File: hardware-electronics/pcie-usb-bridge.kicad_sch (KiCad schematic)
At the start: 41 parts, among them U10 24AA04T-I_OT, U3 PI7C9X440SLBFDE, Y1 ABM8-12.000MHZ-B2-T

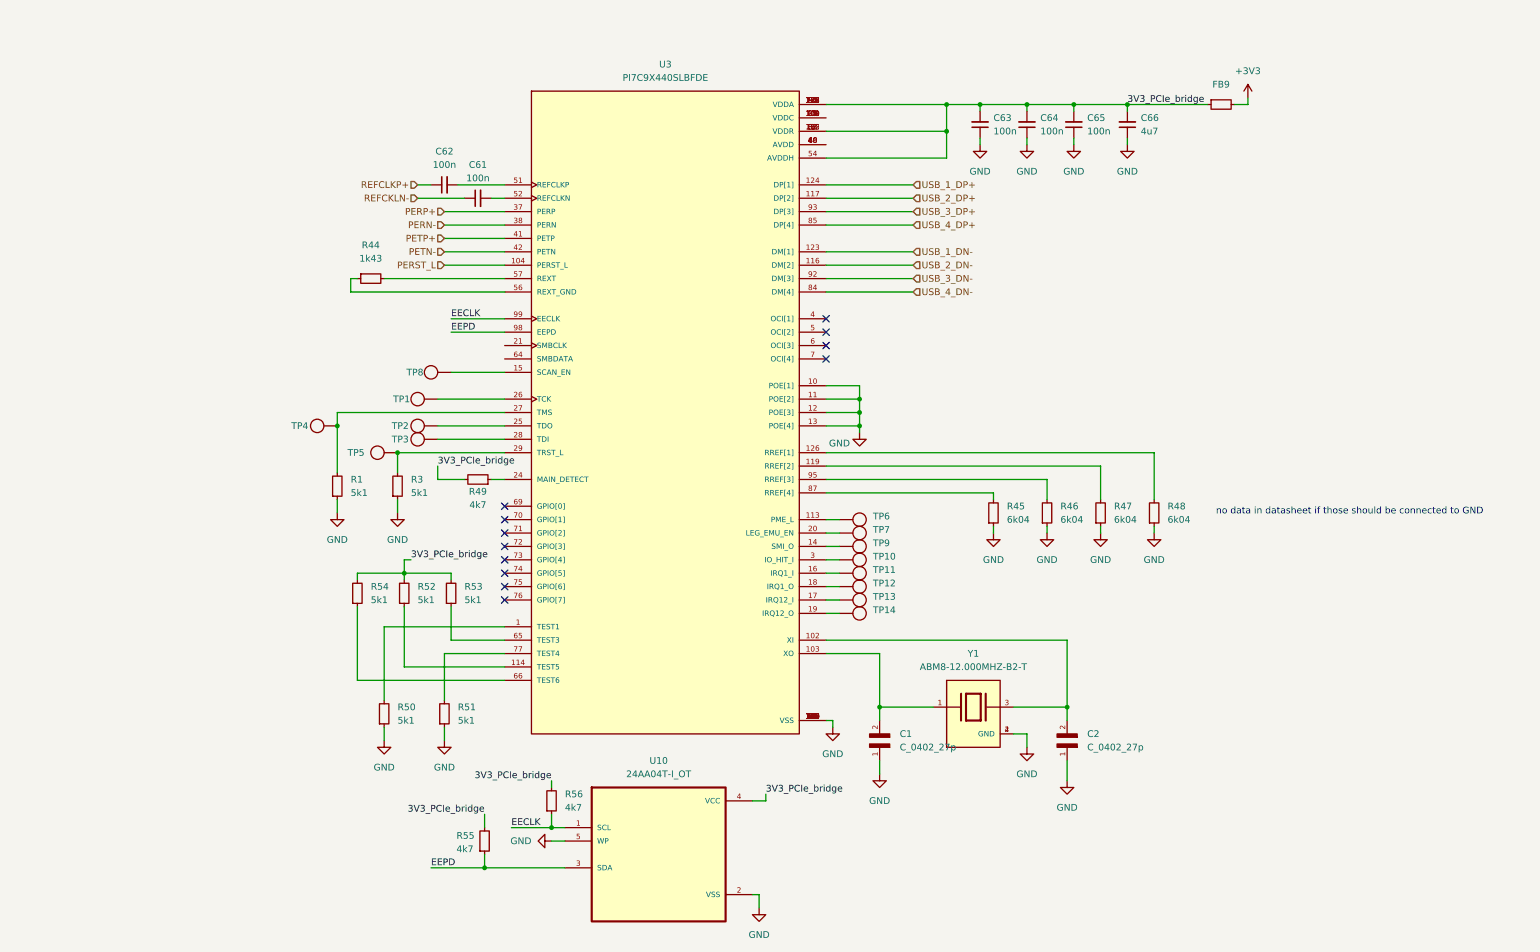
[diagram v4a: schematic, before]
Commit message: [#8] SCH PCIe to USB Update power symbols
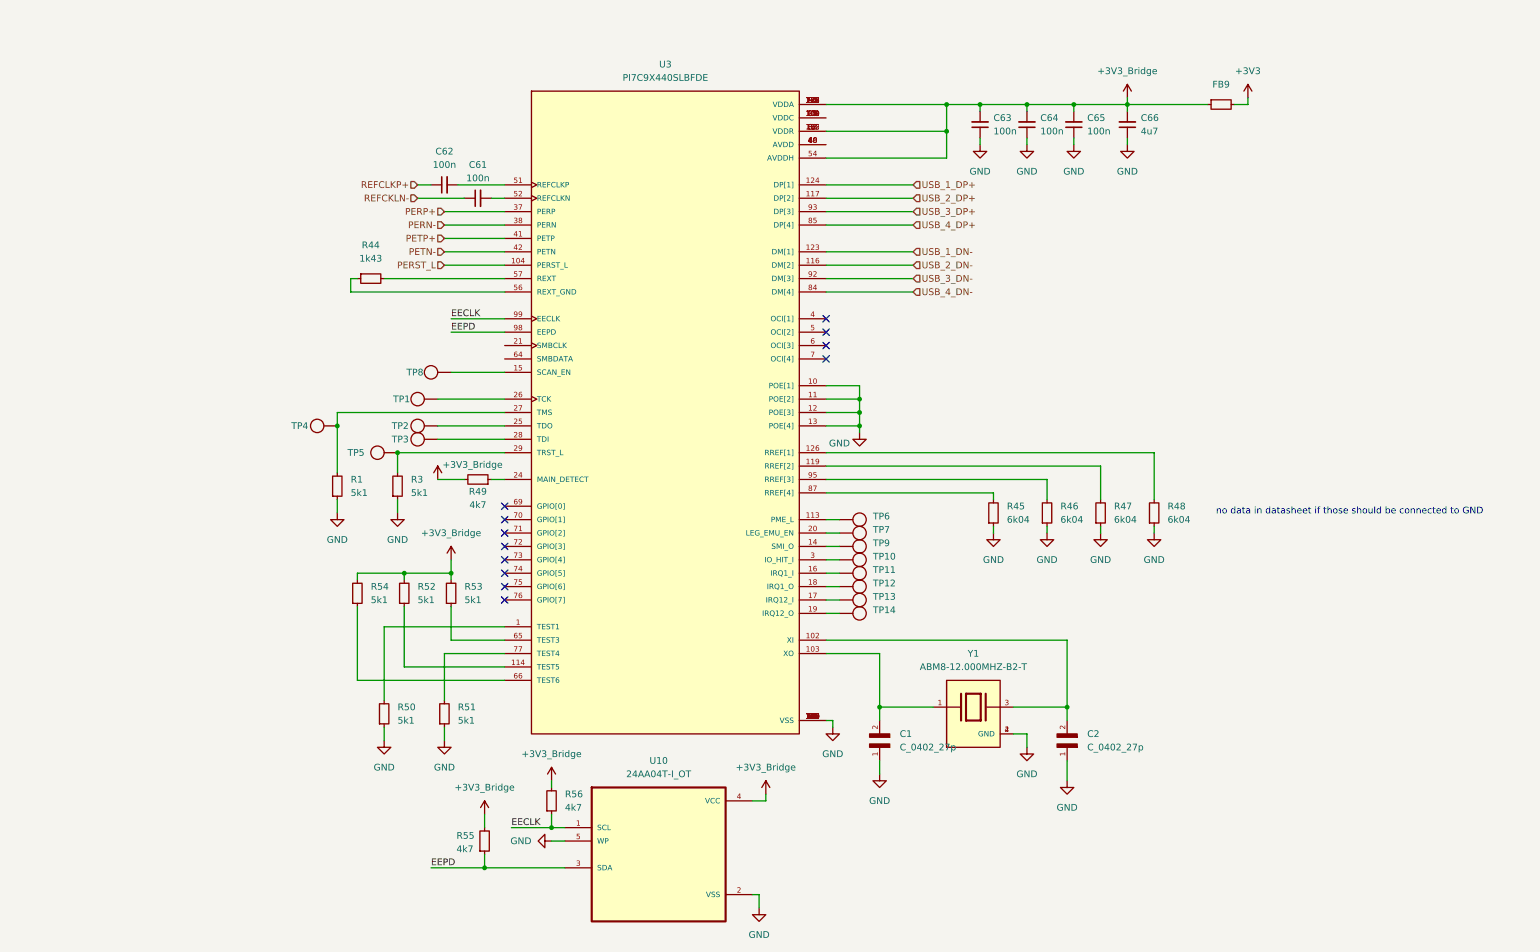
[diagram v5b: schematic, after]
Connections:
- net 3V3_PCIe_bridge renamed +3V3_Bridge

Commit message: [#8] SCH PCIe to USB bridge add series resistors on USB lines
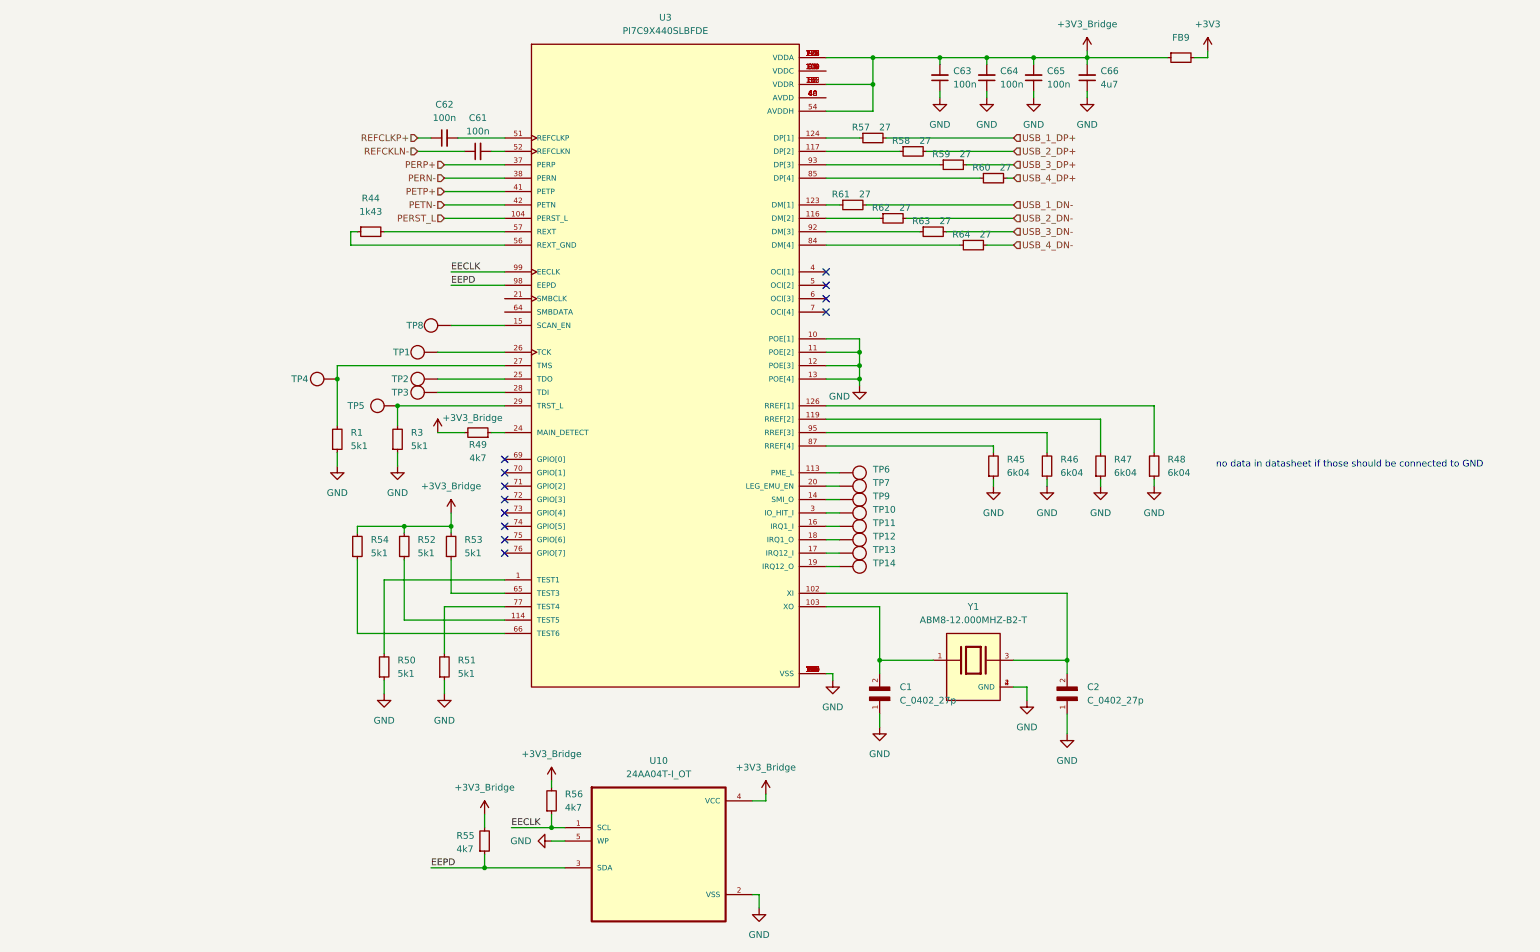
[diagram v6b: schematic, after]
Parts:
- added R57, R58, R59, R60, R61, R62, R63, R64: R_27_0402, M2SmartHomeFootprints:R_0402, symbol M2SmartHomeSymbols:R_27_0402
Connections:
- net USB_1_DN-: now also R61.2; no longer U3.123 (DM[1])
- net USB_1_DP+: now also R57.2; no longer U3.124 (DP[1])
- net USB_2_DN-: now also R62.2; no longer U3.116 (DM[2])
- net USB_2_DP+: now also R58.2; no longer U3.117 (DP[2])
- net USB_3_DN-: now also R63.2; no longer U3.92 (DM[3])
- net USB_3_DP+: now also R59.2; no longer U3.93 (DP[3])
- net USB_4_DN-: now also R64.2; no longer U3.84 (DM[4])
- net USB_4_DP+: now also R60.2; no longer U3.85 (DP[4])
- new net: R64.1, U3.84 (DM[4])
- new net: R60.1, U3.85 (DP[4])
- new net: R61.1, U3.123 (DM[1])
- new net: R57.1, U3.124 (DP[1])
- new net: R63.1, U3.92 (DM[3])
- new net: R58.1, U3.117 (DP[2])
- new net: R62.1, U3.116 (DM[2])
- new net: R59.1, U3.93 (DP[3])
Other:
- moved on the sheet: C1, C2, C61, C62, C63, C64, C65, C66, FB9, R1, R3, R44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

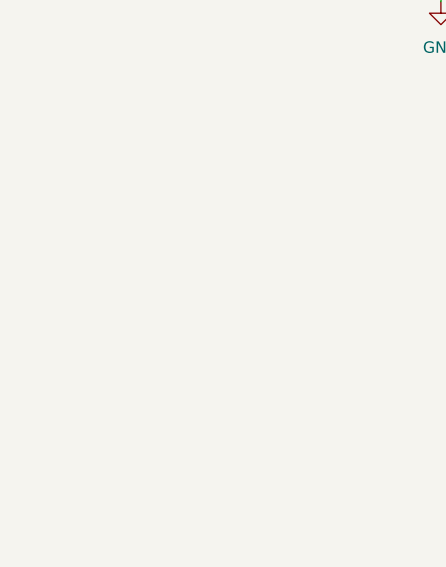
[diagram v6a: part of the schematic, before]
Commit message: [#8] Library add 470nH coil
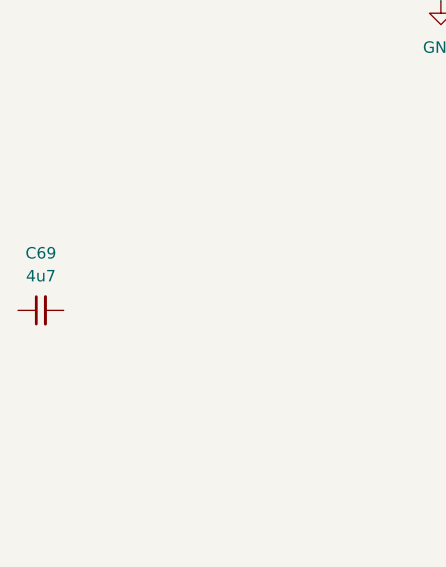
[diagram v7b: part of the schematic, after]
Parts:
- added C69: C_4u7_0402, M2SmartHomeFootprints:C_0402, symbol M2SmartHomeSymbols:C_4u7_0402
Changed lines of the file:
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@@
+	)
+	(symbol
+		(lib_id "M2SmartHomeSymbols:C_4u7_0402")
+		(at 27.94 138.43 0)
+		(unit 1)
+		(exclude_from_sim no)
+		(in_bom yes)
+		(on_board yes)
+		(dnp no)
+		(fields_autoplaced yes)
+		(property "Reference" "C69"
+			(at 30.4863 132.08 0)
+			(effects
+				(font
+					(size 1.27 1.27)
+					(thickness 0.15)
+				)
+			)
+		)
+		(property "Value" "C_4u7_0402"
+			(at 48.26 148.59 0)
+			(effects
+				(font
+					(size 1.27 1.27)
+					(thickness 0.15)
+				)
+				(justify left bottom)
+				(hide yes)
+			)
+		)
+		(property "Footprint" "M2SmartHomeFootprints:C_0402"
+			(at 48.26 151.13 0)
+			(effects
+				(font
+					(size 1.27 1.27)
+					(thickness 0.15)
+				)
+				(justify left bottom)
+				(hide yes)
+			)
+		)
+		(property "Datasheet" "https://www.murata.com/products/productdetail?partno=GRM155R60J475ME47%23"
+			(at 48.26 153.67 0)
+			(effects
+				(font
+					(size 1.27 1.27)
+					(thickness 0.15)
+				)
+				(justify left bottom)
+				(hide yes)
+			)
+		)
+		(property "Description" "SMD Multilayer Ceramic Capacitor, 4.7 µF, 6.3 V, 0402 [1005 Metric], ±20%, X5R, GRM Series"
+			(at 27.94 138.43 0)
+			(effects
+				(font
+					(size 1.27 1.27)
+				)
+				(hide yes)
+			)
+		)
+		(property "MPN" "GRM155R60J475ME47D"
+			(at 48.26 156.21 0)
+			(effects
+				(font
+					(size 1.27 1.27)
+					(thickness 0.15)
+				)
+				(justify left bottom)
+				(hide yes)
+			)
+		)
+		(property "Manufacturer" "Murata"
+			(at 48.26 158.75 0)
+			(effects
+				(font
+					(size 1.27 1.27)
+					(thickness 0.15)
+				)
+				(justify left bottom)
+				(hide yes)
+			)
+		)
+		(property "License" "Apache-2.0"
+			(at 48.26 161.29 0)
+			(effects
+				(font
+					(size 1.27 1.27)
+					(thickness 0.15)
+				)
+				(justify left bottom)
+				(hide yes)
+			)
+		)
+		(property "Author" "Your Name"
+			(at 48.26 163.83 0)
+			(effects
+				(font
+					(size 1.27 1.27)
+					(thickness 0.15)
+				)
+				(justify left bottom)
+				(hide yes)
+			)
+		)
+		(property "Val" "4u7"
+			(at 30.4863 134.62 0)
+			(effects
+				(font
+					(size 1.27 1.27)
+					(thickness 0.15)
+				)
+			)
+		)
+		(property "Voltage" "6.3V"
+			(at 48.26 166.37 0)
+			(effects
+				(font
+					(size 1.27 1.27)
+				)
+				(justify left bottom)
+				(hide yes)
+			)
+		)
+		(property "Dielectric" "X5R"
+			(at 48.26 168.91 0)
+			(effects
+				(font
+					(size 1.27 1.27)
+				)
+				(justify left bottom)
+				(hide yes)
+			)
+		)
+		(pin "2"
+		)
+		(pin "1"
+		)
+		(instances
+			(project "M2SmartHome"
+				(path "/da663dec-9e91-4003-a791-431d460ad63c/d5c056a6-6c83-4beb-8db4-afe66e2a7665"
+					(reference "C69")
+					(unit 1)
+				)
+			)
+		)
 	)
 	(symbol

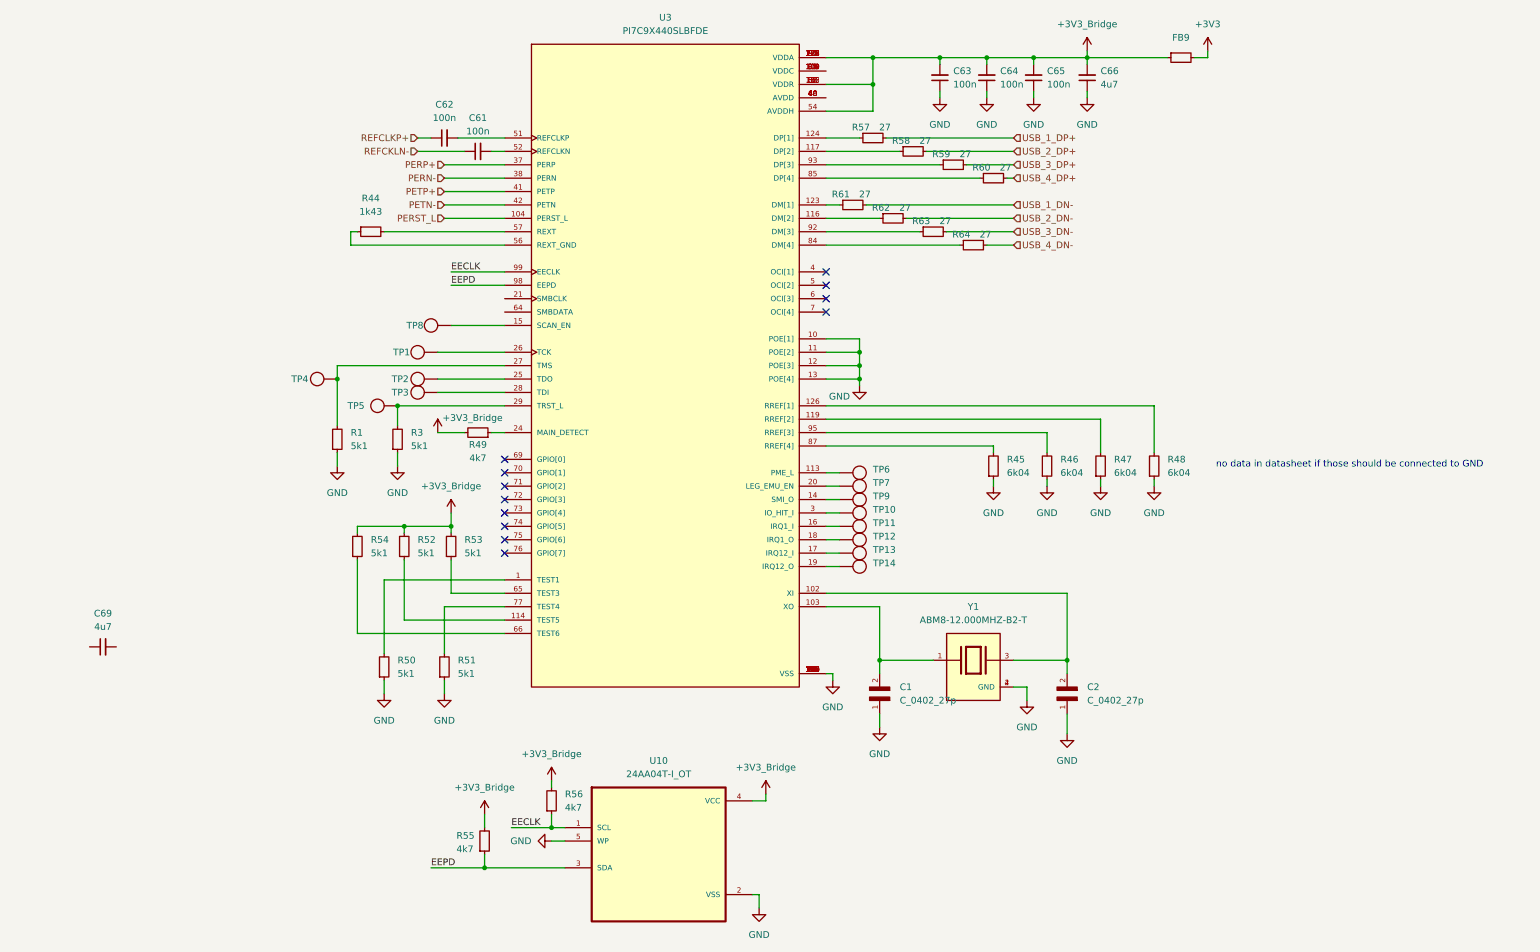
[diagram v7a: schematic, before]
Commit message: [#8] SCH PCIe to USB Add 1V0 DCDC converter
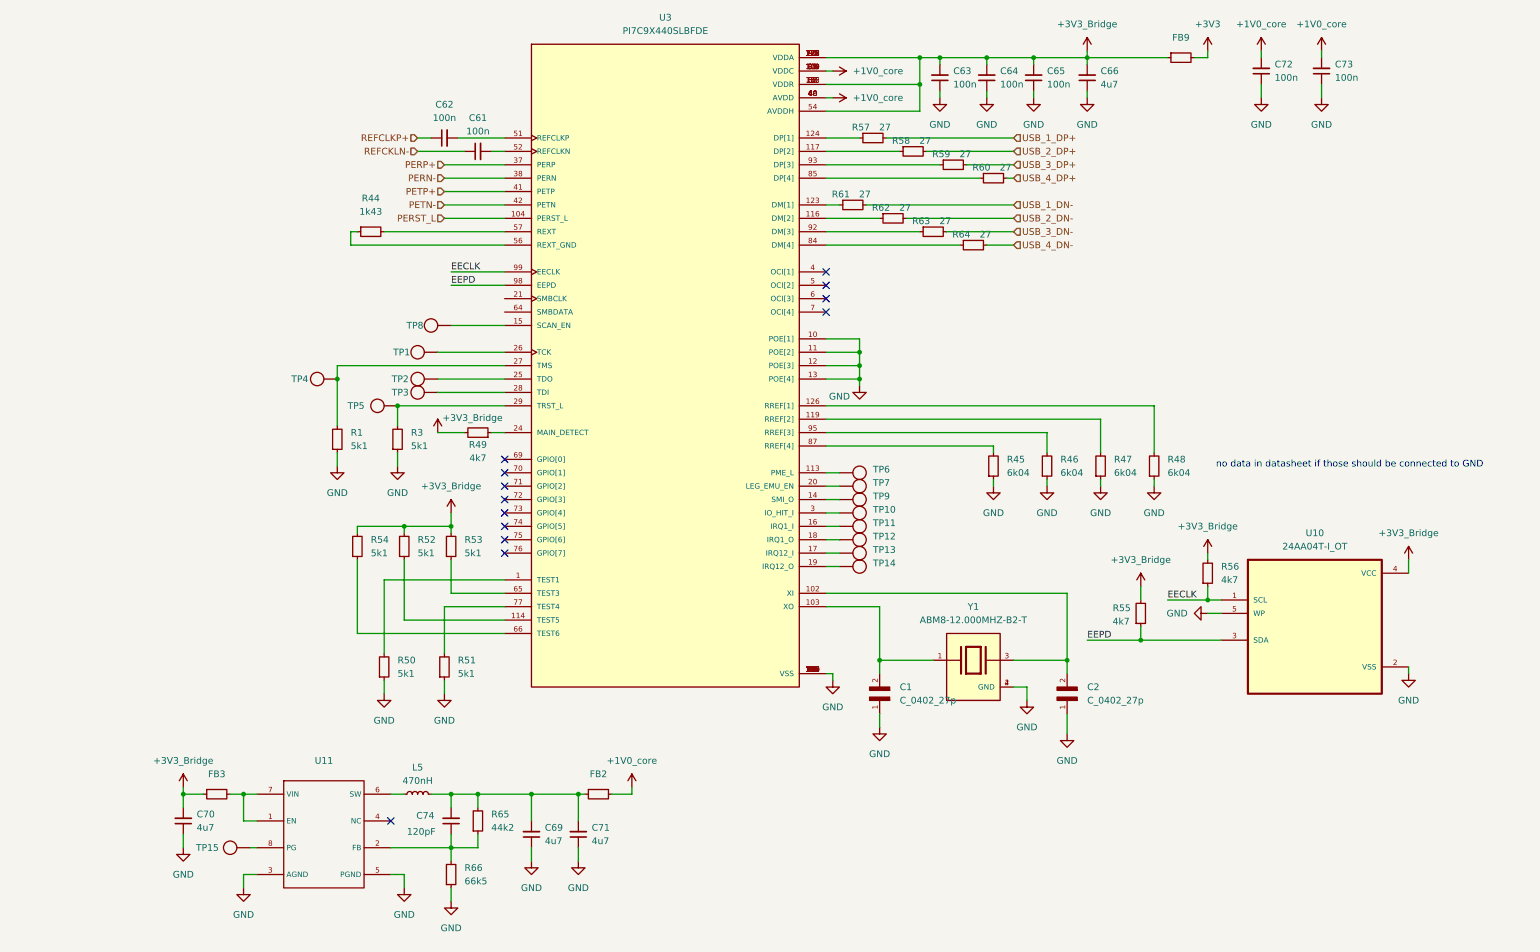
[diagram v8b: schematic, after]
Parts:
- added C70, C71: C_4u7_0402, M2SmartHomeFootprints:C_0402, symbol M2SmartHomeSymbols:C_4u7_0402
- added C72, C73: C_100n_0402, M2SmartHomeFootprints:C_0402, symbol M2SmartHomeSymbols:C_100n_0402
- added C74: C_120pF_0402, M2SmartHomeFootprints:C_0402, symbol M2SmartHomeSymbols:C_120pF_0402
- added FB2, FB3: FB_120R_0603, M2SmartHomeFootprints:FB_0603, symbol M2SmartHomeSymbols:FB_120R_0603
- added L5: L_470nH_XFL4015, M2SmartHomeFootprints:XFL4015-471MEB, symbol M2SmartHomeSymbols:L_470nH_XFL4015
- added R65: R_44k2_0402, M2SmartHomeFootprints:R_0402, symbol M2SmartHomeSymbols:R_44k2_0402
- added R66: R_66k5_0402, R_66k5_0402:R_0402_1005Metric, symbol M2SmartHomeSymbols:R_66k5_0402
- added TP15: ~, symbol M2SmartHomeSymbols:TP_SMD_1mm
- added U11: ~, M2SmartHomeFootprints:TPS62822DLCR, symbol M2SmartHomeSymbols:TPS62822DLCR
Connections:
- net +3V3_Bridge: now also C70.2, FB3.1
- net GND: now also C69.1, C70.1, C71.1, C72.1, C73.1, R66.1, U11.3 (AGND), U11.5 (PGND)
- net +1V0_core: now reaches U3.100 (VDDC), U3.109 (VDDC), U3.111 (VDDC), U3.22 (VDDC), U3.35 (VDDC), U3.81 (VDDC)
- net +1V0_core: now also U3.40 (AVDD), U3.46 (AVDD), U3.49 (AVDD), U3.60 (AVDD), C72.2, C73.2, FB2.2
- net at C69.2: now also C71.2, C74.2, FB2.1, L5.2, R65.2
- new net: C74.1, R65.1, R66.2, U11.2 (FB)
- new net: FB3.2, U11.1 (EN), U11.7 (VIN)
- new net: L5.1, U11.6 (SW)
- new net: TP15., U11.8 (PG)
- no-connect marks 12 -> 13
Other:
- moved on the sheet: R55, R56, U10
